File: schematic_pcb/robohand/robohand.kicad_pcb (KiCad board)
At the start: 2 copper layers, 54 x 57.5 mm, 11 parts, among them M1 Motor_Servo, M2 Motor_Servo, M3 Motor_Servo, M4 Motor_Servo, M5 Motor_Servo, SW1 SW_SPST, SW2 SW_SPST, SW3 SW_SPST, U1 ESP32-CAM

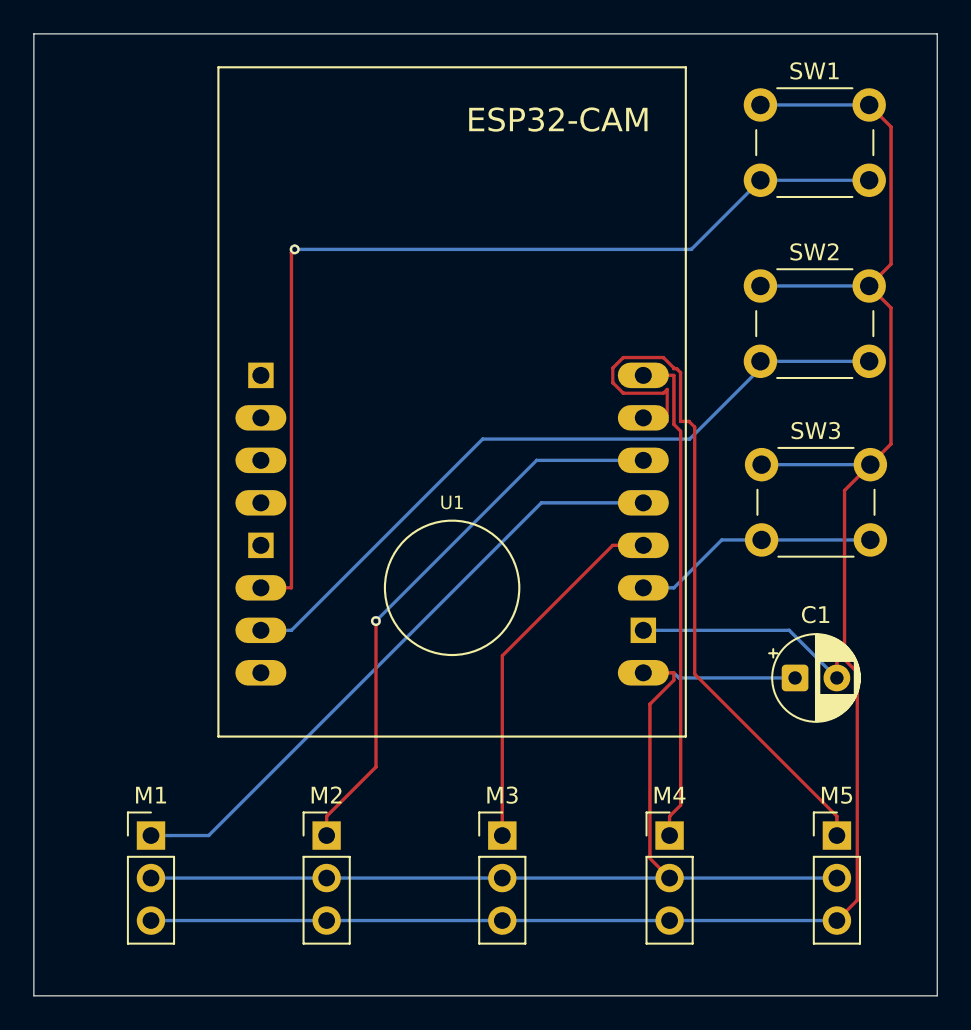
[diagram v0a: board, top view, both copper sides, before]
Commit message: edited readme and fixed esp32 library issue
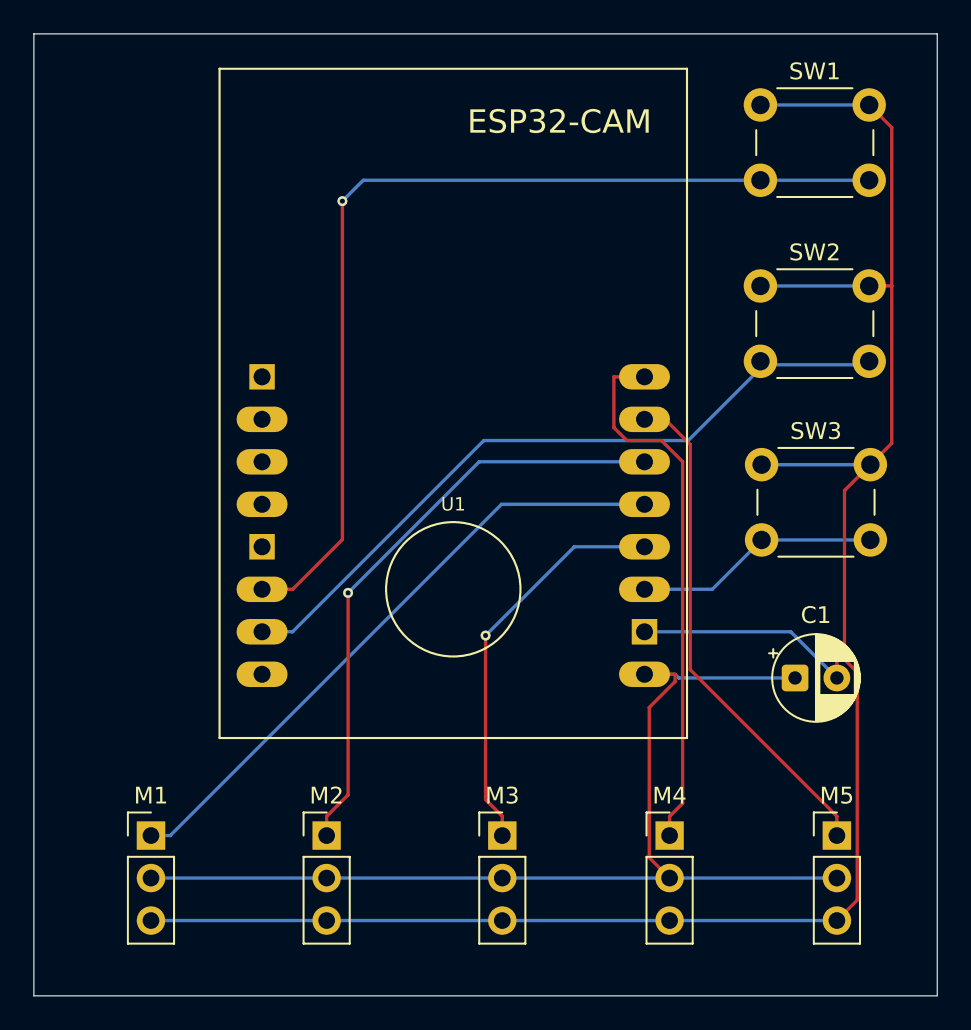
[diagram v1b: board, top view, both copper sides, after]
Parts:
- moved U1 0.11 mm to (148.6, 95.1)
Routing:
- net Net-(M5-PWM): track 44.4 -> 30.5 mm
- net Net-(M4-PWM): track 29.8 -> 32.5 mm
- net Net-(M3-PWM): track 21.9 -> 24.1 mm, vias 0 -> 1
- net Net-(M2-PWM): track 34.2 -> 36.0 mm
- net Net-(SW1-B): track 59.3 -> 58.3 mm
